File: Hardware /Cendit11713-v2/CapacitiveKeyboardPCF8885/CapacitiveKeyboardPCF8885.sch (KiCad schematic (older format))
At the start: 58 parts

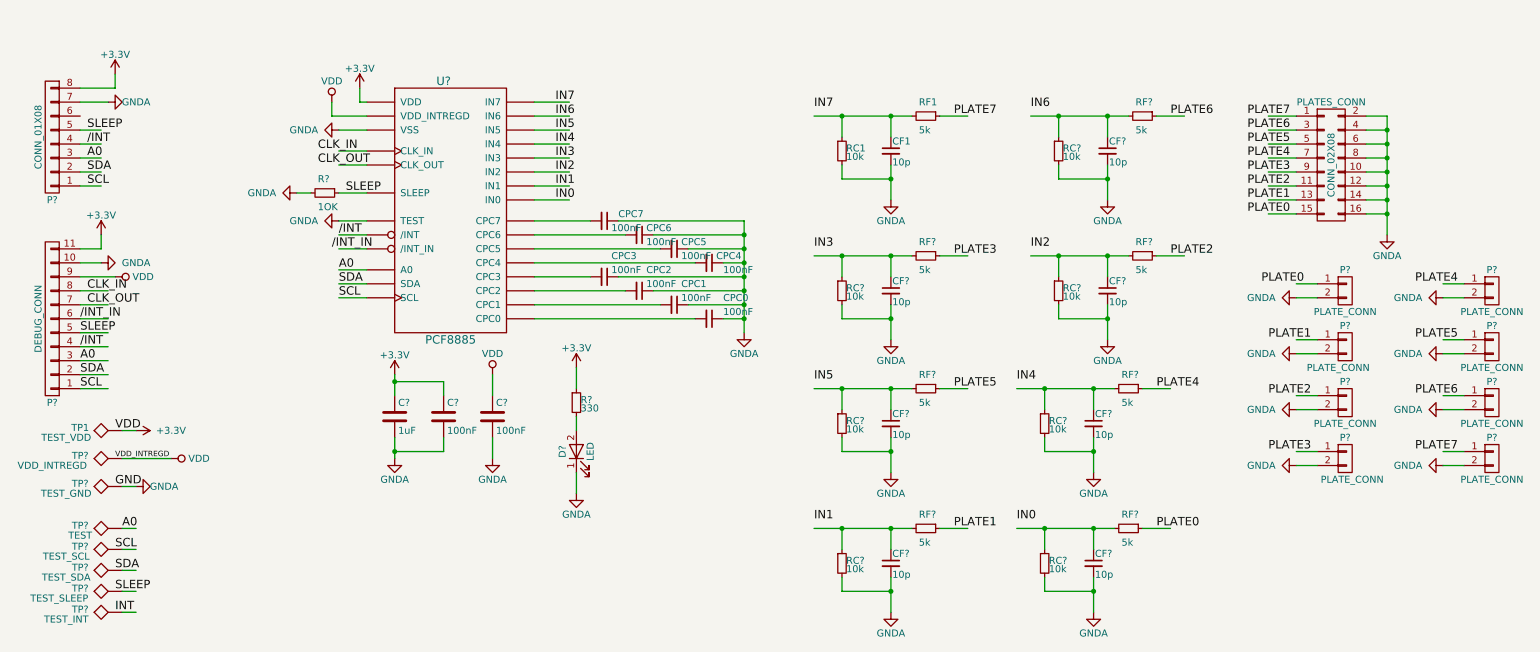
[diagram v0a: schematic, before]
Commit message: Trabajo en CenditLab.Reducido + Cendit17713 PCB
  - Clases paneles UI modificados
  - Clases para manejo y validacion de datos
  - PCB expansor puertos Viking
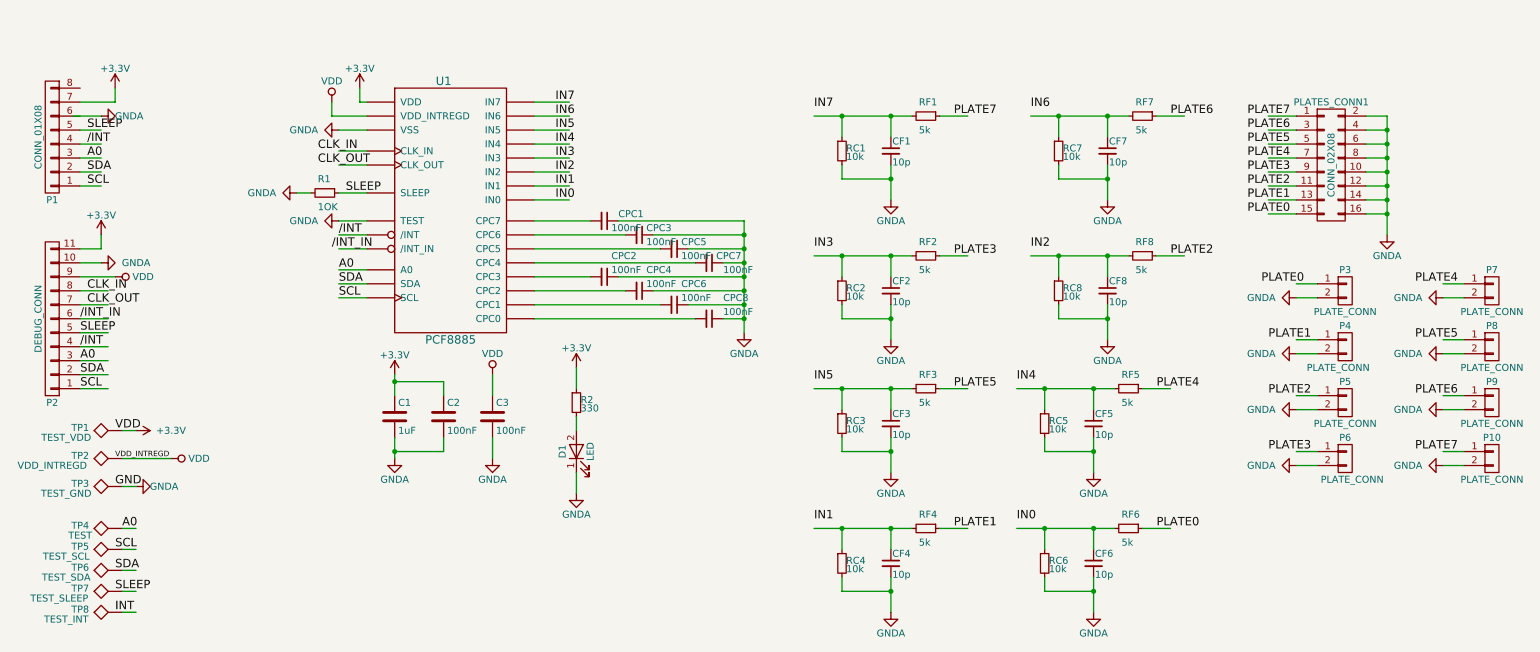
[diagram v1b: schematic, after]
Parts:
- U1: renamed from U?; footprint (none) -> LibKicad:PCF8885TS
- gave numbers to parts that had none: 44
- renumbered CPC7 to CPC1, CPC3 to CPC2, CPC6 to CPC3, CPC2 to CPC4, CPC1 to CPC6, CPC4 to CPC7, CPC0 to CPC8, PLATES_CONN to PLATES_CONN1

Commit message: Trabajo en CenditLab + Cendit11713 PCB
  - Clases UI entrada de ENR + archivos fxml
  - Expansor puertos Viking
  - Controlador teclado capacitivo
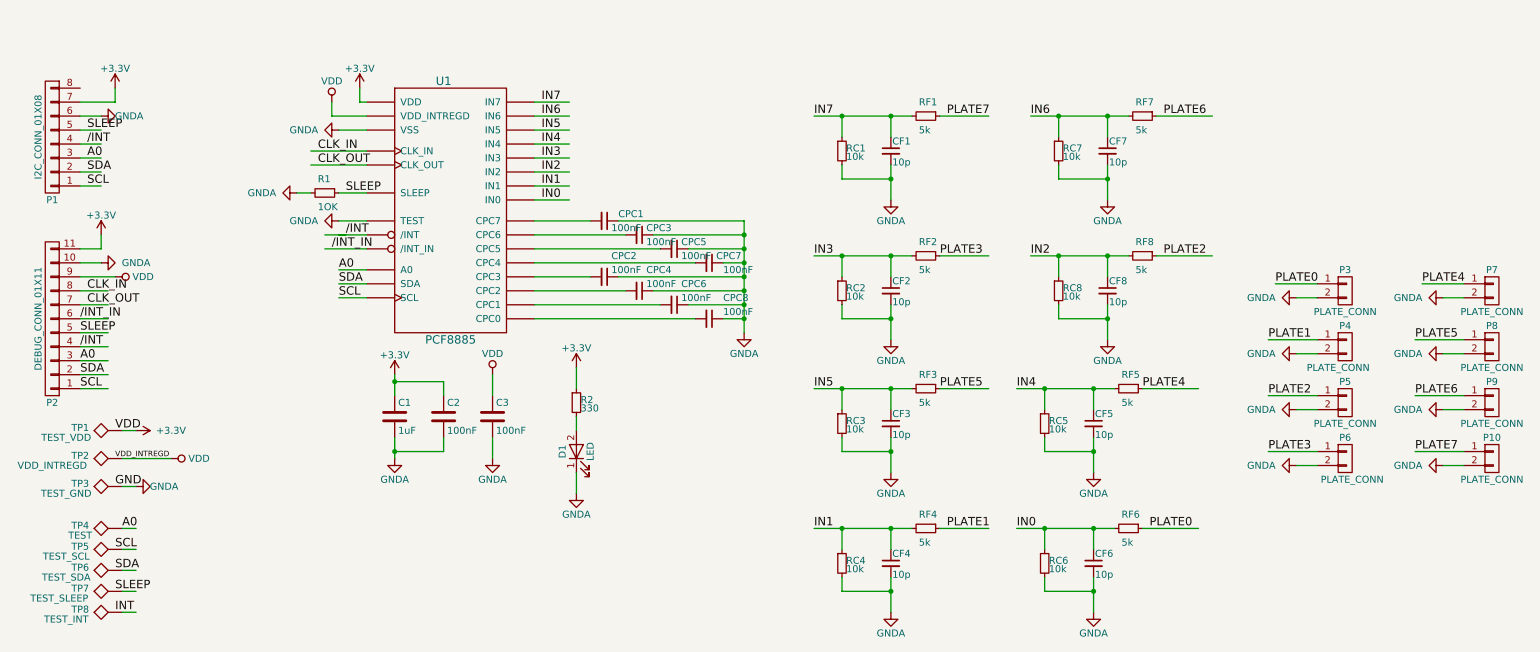
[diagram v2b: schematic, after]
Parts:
- removed PLATES_CONN1: CONN_02X08, symbol CONN_02X08
- C1, C2, C3, CF1, CF2, CF3, CF4, CF5, CF6, CF7, CF8, CPC1, CPC2, CPC3, CPC4, CPC5, CPC6, CPC7, CPC8: footprint (none) -> Capacitors_SMD:C_0805_HandSoldering
- D1: footprint (none) -> LEDs:LED_0805
- P1: value CONN_01X08 -> I2C_CONN_01X08; footprint (none) -> CenditFootprints:SLIMLINE_SATA_PLUG_7P_6P
- P10, P3, P4, P5, P6, P7, P8, P9: footprint (none) -> Pin_Headers:Pin_Header_Straight_1x02
- P2: value DEBUG_CONN -> DEBUG_CONN_01X11; footprint (none) -> Pin_Headers:Pin_Header_Straight_1x11
- R1, R2, RC1, RC2, RC3, RC4, RC5, RC6, RC7, RC8, RF1, RF2, RF3, RF4, RF5, RF6, RF7, RF8: footprint (none) -> Resistors_SMD:R_0805_HandSoldering
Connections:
- wire segments 168 -> 152

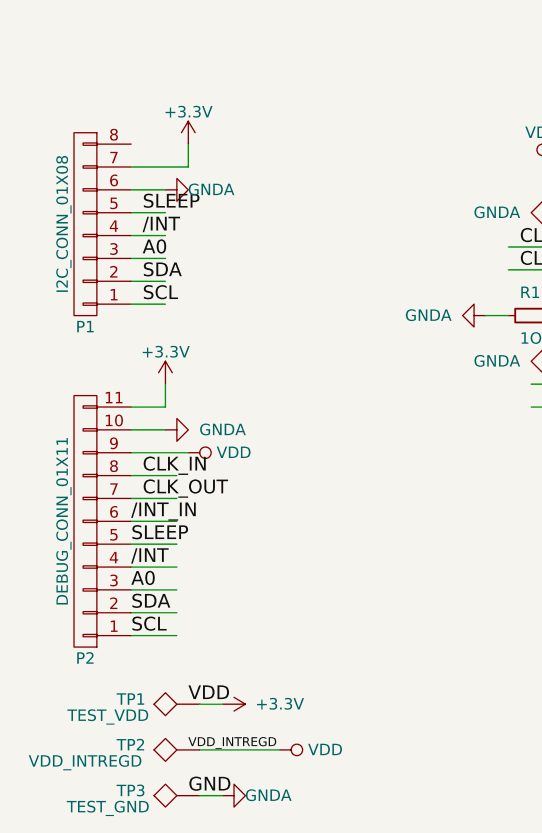
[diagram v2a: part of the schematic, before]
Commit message: Trabajo en CenditLab.Reducido + Cendit11713 PCB
   - CenditLab clases para manejo de setup ENR
   - Clase field para dato temperatura
   - Edición de PCBs Capacitive Keyboard
   - Edición de esquematico MainBoard con PIC18F4550 DIP
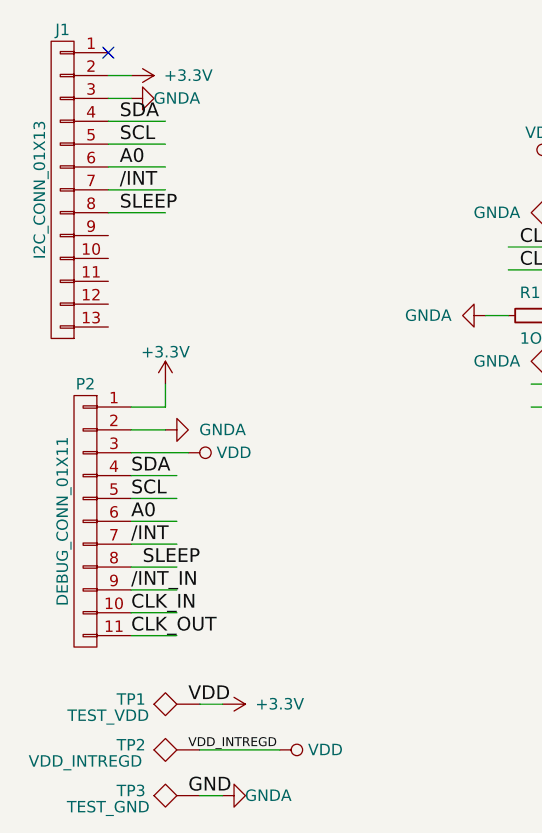
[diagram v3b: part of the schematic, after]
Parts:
- removed P1: I2C_CONN_01X08, CenditFootprints:SLIMLINE_SATA_PLUG_7P_6P, symbol CONN_01X08
- added J1: I2C_CONN_01X13, CenditFootprints:SLIMLINE_SATA_PLUG_7P_6P, symbol CONN_01X13
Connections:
- wire segments 152 -> 151
- no-connect marks 0 -> 1
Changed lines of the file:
@@
 LIBS:contrib
 LIBS:valves
-LIBS:CenditBasic
 LIBS:CapacitiveKeyboardPCF8885-cache
 EELAYER 25 0
@@
 $EndComp
 $Comp
-L GNDA #PWR012
+L GNDA #PWR011
 U 1 1 59CC7E9D
 P 2800 2050
-F 0 "#PWR012" H 2800 1800 50  0001 C CNN
+F 0 "#PWR011" H 2800 1800 50  0001 C CNN
 F 1 "GNDA" V 2800 1800 50  0000 C CNN
 F 2 "" H 2800 2050 50  0000 C CNN
@@
 $EndComp
 $Comp
-L +3.3V #PWR013
+L +3.3V #PWR012
 U 1 1 59CC8C35
 P 2950 1100
-F 0 "#PWR013" H 2950 950 50  0001 C CNN
+F 0 "#PWR012" H 2950 950 50  0001 C CNN
 F 1 "+3.3V" H 2950 1240 50  0000 C CNN
 F 2 "" H 2950 1100 50  0000 C CNN
@@
 $EndComp
 $Comp
-L VDD #PWR014
+L VDD #PWR013
 U 1 1 59CC8CA3
 P 2750 1200
-F 0 "#PWR014" H 2750 1050 50  0001 C CNN
+F 0 "#PWR013" H 2750 1050 50  0001 C CNN
 F 1 "VDD" H 2750 1350 50  0000 C CNN
 F 2 "" H 2750 1200 50  0000 C CNN
@@
 $EndComp
 $Comp
-L +3.3V #PWR015
+L +3.3V #PWR014
 U 1 1 59CCAF94
 P 3200 3150
-F 0 "#PWR015" H 3200 3000 50  0001 C CNN
+F 0 "#PWR014" H 3200 3000 50  0001 C CNN
 F 1 "+3.3V" H 3200 3290 50  0000 C CNN
 F 2 "" H 3200 3150 50  0000 C CNN
@@
 $EndComp
 $Comp
-L VDD #PWR016
+L VDD #PWR015
 U 1 1 59CCB002
 P 3900 3150
-F 0 "#PWR016" H 3900 3000 50  0001 C CNN
+F 0 "#PWR015" H 3900 3000 50  0001 C CNN
 F 1 "VDD" H 3900 3300 50  0000 C CNN
 F 2 "" H 3900 3150 50  0000 C CNN
@@
 $EndComp
 $Comp
-L GNDA #PWR017
+L GNDA #PWR016
 U 1 1 59CCB3D4
 P 3200 3750
-F 0 "#PWR017" H 3200 3500 50  0001 C CNN
+F 0 "#PWR016" H 3200 3500 50  0001 C CNN
 F 1 "GNDA" H 3200 3600 50  0000 C CNN
 F 2 "" H 3200 3750 50  0000 C CNN
@@
 $EndComp
 $Comp
-L GNDA #PWR018
+L GNDA #PWR017
 U 1 1 59CCB46F
 P 3900 3750
-F 0 "#PWR018" H 3900 3500 50  0001 C CNN
+F 0 "#PWR017" H 3900 3500 50  0001 C CNN
 F 1 "GNDA" H 3900 3600 50  0000 C CNN
 F 2 "" H 3900 3750 50  0000 C CNN
@@
 $EndComp
 $Comp
-L GNDA #PWR019
+L GNDA #PWR018
 U 1 1 59CDAF81
 P 9650 3800
-F 0 "#PWR019" H 9650 3550 50  0001 C CNN
+F 0 "#PWR018" H 9650 3550 50  0001 C CNN
 F 1 "GNDA" V 9650 3550 50  0000 C CNN
 F 2 "" H 9650 3800 50  0000 C CNN
@@
 $EndComp
 $Comp
-L GNDA #PWR020
+L GNDA #PWR019
 U 1 1 59CDAFEF
 P 9650 3400
-F 0 "#PWR020" H 9650 3150 50  0001 C CNN
+F 0 "#PWR019" H 9650 3150 50  0001 C CNN
 F 1 "GNDA" V 9650 3150 50  0000 C CNN
 F 2 "" H 9650 3400 50  0000 C CNN
@@
 $EndComp
 $Comp
-L GNDA #PWR021
+L GNDA #PWR020
 U 1 1 59CDB364
 P 9650 3000
-F 0 "#PWR021" H 9650 2750 50  0001 C CNN
+F 0 "#PWR020" H 9650 2750 50  0001 C CNN
 F 1 "GNDA" V 9650 2750 50  0000 C CNN
 F 2 "" H 9650 3000 50  0000 C CNN
@@
 $EndComp
 $Comp
-L GNDA #PWR022
+L GNDA #PWR021
 U 1 1 59CDB3D2
 P 9650 2600
-F 0 "#PWR022" H 9650 2350 50  0001 C CNN
+F 0 "#PWR021" H 9650 2350 50  0001 C CNN
 F 1 "GNDA" V 9650 2350 50  0000 C CNN
 F 2 "" H 9650 2600 50  0000 C CNN
@@
 $EndComp
 $Comp
-L GNDA #PWR023
+L GNDA #PWR022
 U 1 1 59CDBC01
 P 10700 2600
-F 0 "#PWR023" H 10700 2350 50  0001 C CNN
+F 0 "#PWR022" H 10700 2350 50  0001 C CNN
 F 1 "GNDA" V 10700 2350 50  0000 C CNN
 F 2 "" H 10700 2600 50  0000 C CNN
@@
 $EndComp
 $Comp
-L GNDA #PWR024
+L GNDA #PWR023
 U 1 1 59CDBC6F
 P 10700 3000
-F 0 "#PWR024" H 10700 2750 50  0001 C CNN
+F 0 "#PWR023" H 10700 2750 50  0001 C CNN
 F 1 "GNDA" V 10700 2750 50  0000 C CNN
 F 2 "" H 10700 3000 50  0000 C CNN
@@
 $EndComp
 $Comp
-L GNDA #PWR025
+L GNDA #PWR024
 U 1 1 59CDBD37
 P 10700 3400
-F 0 "#PWR025" H 10700 3150 50  0001 C CNN
+F 0 "#PWR024" H 10700 3150 50  0001 C CNN
 F 1 "GNDA" V 10700 3150 50  0000 C CNN
 F 2 "" H 10700 3400 50  0000 C CNN
@@
 $EndComp
 $Comp
-L GNDA #PWR026
+L GNDA #PWR025
 U 1 1 59CDBDFF
 P 10700 3800
-F 0 "#PWR026" H 10700 3550 50  0001 C CNN
+F 0 "#PWR025" H 10700 3550 50  0001 C CNN
 F 1 "GNDA" V 10700 3550 50  0000 C CNN
 F 2 "" H 10700 3800 50  0000 C CNN
@@
 PLATE7
 $Comp
-L CONN_01X08 P1
-U 1 1 59CE24CF
-P 750 1450
-F 0 "P1" H 750 1900 50  0000 C CNN
-F 1 "I2C_CONN_01X08" V 850 1450 50  0000 C CNN
-F 2 "CenditFootprints:SLIMLINE_SATA_PLUG_7P_6P" H 750 1450 50  0001 C CNN
-F 3 "" H 750 1450 50  0000 C CNN
-	1    750  1450
-	-1   0    0    1
-$EndComp
-$Comp
 L CONN_01X11 P2
 U 1 1 59CE30AA
@@
 F 3 "" H 750 2750 50  0000 C CNN
 	1    750  2750
-	-1   0    0    1
-$EndComp
-$Comp
-L GNDA #PWR027
+	-1   0    0    -1
+$EndComp
+$Comp
+L GNDA #PWR026
 U 1 1 59CE507F
-P 1100 1300
-F 0 "#PWR027" H 1100 1050 50  0001 C CNN
-F 1 "GNDA" V 1100 1100 50  0000 C CNN
-F 2 "" H 1100 1300 50  0000 C CNN
-F 3 "" H 1100 1300 50  0000 C CNN
-	1    1100 1300
+P 950 900
+F 0 "#PWR026" H 950 650 50  0001 C CNN
+F 1 "GNDA" V 950 700 50  0000 C CNN
+F 2 "" H 950 900 50  0000 C CNN
+F 3 "" H 950 900 50  0000 C CNN
+	1    950  900
 	0    -1   -1   0
 $EndComp
 $Comp
-L +3.3V #PWR028
+L +3.3V #PWR027
 U 1 1 59CE5337
-P 1200 1100
-F 0 "#PWR028" H 1200 950 50  0001 C CNN
-F 1 "+3.3V" H 1200 1240 50  0000 C CNN
-F 2 "" H 1200 1100 50  0000 C CNN
-F 3 "" H 1200 1100 50  0000 C CNN
-	1    1200 1100
-	1    0    0    -1
-$EndComp
-Text Label 1000 1800 0    60   ~ 0
+P 950 800
+F 0 "#PWR027" H 950 650 50  0001 C CNN
+F 1 "+3.3V" V 950 1050 50  0000 C CNN
+F 2 "" H 950 800 50  0000 C CNN
+F 3 "" H 950 800 50  0000 C CNN
+	1    950  800
+	0    1    1    0
+$EndComp
+Text Label 900  1100 0    60   ~ 0
 SCL
-Text Label 1000 1700 0    60   ~ 0
+Text Label 900  1000 0    60   ~ 0
 SDA
-Text Label 1000 1600 0    60   ~ 0
+Text Label 900  1200 0    60   ~ 0
 A0
-Text Label 1000 1500 0    60   ~ 0
+Text Label 900  1300 0    60   ~ 0
 /INT
-Text Label 1000 1400 0    60   ~ 0
+Text Label 900  1400 0    60   ~ 0
 SLEEP
 $Comp
@@
 $EndComp
 $Comp
-L GNDA #PWR029
+L GNDA #PWR028
 U 1 1 59CE74DE
 P 2500 1850
-F 0 "#PWR029" H 2500 1600 50  0001 C CNN
+F 0 "#PWR028" H 2500 1600 50  0001 C CNN
 F 1 "GNDA" V 2500 1600 50  0000 C CNN
 F 2 "" H 2500 1850 50  0000 C CNN
@@
 SLEEP
 $Comp
-L +3.3V #PWR030
+L +3.3V #PWR029
 U 1 1 59CEC609
 P 1100 2150
-F 0 "#PWR030" H 1100 2000 50  0001 C CNN
+F 0 "#PWR029" H 1100 2000 50  0001 C CNN
 F 1 "+3.3V" H 1100 2290 50  0000 C CNN
 F 2 "" H 1100 2150 50  0000 C CNN
@@
 $EndComp
 $Comp
-L GNDA #PWR031
+L GNDA #PWR030
 U 1 1 59CEC67D
 P 1100 2350
-F 0 "#PWR031" H 1100 2100 50  0001 C CNN
+F 0 "#PWR030" H 1100 2100 50  0001 C CNN
 F 1 "GNDA" V 1100 2100 50  0000 C CNN
 F 2 "" H 1100 2350 50  0000 C CNN
@@
 $EndComp
 $Comp
-L VDD #PWR032
+L VDD #PWR031
 U 1 1 59CECB1B
 P 1200 2450
-F 0 "#PWR032" H 1200 2300 50  0001 C CNN
+F 0 "#PWR031" H 1200 2300 50  0001 C CNN
 F 1 "VDD" V 1200 2650 50  0000 C CNN
 F 2 "" H 1200 2450 50  0000 C CNN
@@
 Text Label 2650 1550 0    60   ~ 0
 CLK_IN
+Text Label 950  2650 0    60   ~ 0
+SCL
+Text Label 950  2550 0    60   ~ 0
+SDA
+Text Label 950  2750 0    60   ~ 0
+A0
+Text Label 950  2850 0    60   ~ 0
+/INT
+Text Label 1000 2950 0    60   ~ 0
+SLEEP
+Text Label 950  3050 0    60   ~ 0
+/INT_IN
+Text Label 950  3150 0    60   ~ 0
+CLK_IN
 Text Label 950  3250 0    60   ~ 0
-SCL
-Text Label 950  3150 0    60   ~ 0
-SDA
-Text Label 950  3050 0    60   ~ 0
-A0
-Text Label 950  2950 0    60   ~ 0
-/INT
-Text Label 950  2850 0    60   ~ 0
-SLEEP
-Text Label 950  2750 0    60   ~ 0
-/INT_IN
-Text Label 1000 2550 0    60   ~ 0
-CLK_IN
-Text Label 1000 2650 0    60   ~ 0
 CLK_OUT
 $Comp
@@
 $EndComp
 $Comp
-L +3.3V #PWR033
+L +3.3V #PWR032
 U 1 1 59CFAFA9
 P 4500 3100
-F 0 "#PWR033" H 4500 2950 50  0001 C CNN
+F 0 "#PWR032" H 4500 2950 50  0001 C CNN
 F 1 "+3.3V" H 4500 3240 50  0000 C CNN
 F 2 "" H 4500 3100 50  0000 C CNN
@@
 $EndComp
 $Comp
-L GNDA #PWR034
+L GNDA #PWR033
 U 1 1 59CFB085
 P 4500 4000
-F 0 "#PWR034" H 4500 3750 50  0001 C CNN
+F 0 "#PWR033" H 4500 3750 50  0001 C CNN
 F 1 "GNDA" H 4500 3850 50  0000 C CNN
 F 2 "" H 4500 4000 50  0000 C CNN
@@
 GND
 $Comp
-L GNDA #PWR035
+L GNDA #PWR034
 U 1 1 59D0D18F
 P 1350 3950
-F 0 "#PWR035" H 1350 3700 50  0001 C CNN
+F 0 "#PWR034" H 1350 3700 50  0001 C CNN
 F 1 "GNDA" V 1350 3750 50  0000 C CNN
 F 2 "" H 1350 3950 50  0000 C CNN
@@
 $EndComp
 $Comp
-L +3.3V #PWR036
+L +3.3V #PWR035
 U 1 1 59D0D3EE
 P 1350 3550
-F 0 "#PWR036" H 1350 3400 50  0001 C CNN
+F 0 "#PWR035" H 1350 3400 50  0001 C CNN
 F 1 "+3.3V" V 1350 3800 50  0000 C CNN
 F 2 "" H 1350 3550 50  0000 C CNN
@@
 $EndComp
 $Comp
-L VDD #PWR037
+L VDD #PWR036
 U 1 1 59D0D5CE
 P 1600 3750
-F 0 "#PWR037" H 1600 3600 50  0001 C CNN
+F 0 "#PWR036" H 1600 3600 50  0001 C CNN
 F 1 "VDD" V 1600 3950 50  0000 C CNN
 F 2 "" H 1600 3750 50  0000 C CNN
@@
 	9800 2600 9650 2600
 Wire Wire Line
-	950  1200 1200 1200
-Wire Wire Line
-	950  1400 1100 1400
-Wire Wire Line
-	950  1500 1100 1500
-Wire Wire Line
-	950  1600 1100 1600
-Wire Wire Line
-	950  1700 1100 1700
-Wire Wire Line
-	950  1800 1100 1800
-Wire Wire Line
 	2600 1550 3000 1550
 Wire Wire Line
@@
 	3000 2600 2800 2600
 Wire Wire Line
-	1200 1200 1200 1100
-Wire Wire Line
 	2800 1850 3000 1850
 Wire Wire Line
@@
 	2850 2150 2700 2150
 Wire Wire Line
-	1100 1300 950  1300
-Wire Wire Line
 	10850 3700 10500 3700
 Wire Wire Line
 	10850 2500 10550 2500
+NoConn ~ 850  700
+$Comp
+L CONN_01X13 J1
+U 1 1 59E66F43
+P 650 1300
+F 0 "J1" H 650 2000 50  0000 C CNN
+F 1 "I2C_CONN_01X13" V 750 1300 50  0000 C CNN
+F 2 "CenditFootprints:SLIMLINE_SATA_PLUG_7P_6P" H 650 1300 50  0001 C CNN
+F 3 "" H 650 1300 50  0001 C CNN
+	1    650  1300
+	-1   0    0    -1
+$EndComp
+Wire Wire Line
+	850  800  950  800
+Wire Wire Line
+	850  900  950  900
+Wire Wire Line
+	850  1000 1100 1000
+Wire Wire Line
+	850  1100 1100 1100
+Wire Wire Line
+	850  1200 1100 1200
+Wire Wire Line
+	850  1300 1100 1300
+Wire Wire Line
+	850  1400 1100 1400
 $EndSCHEMATC

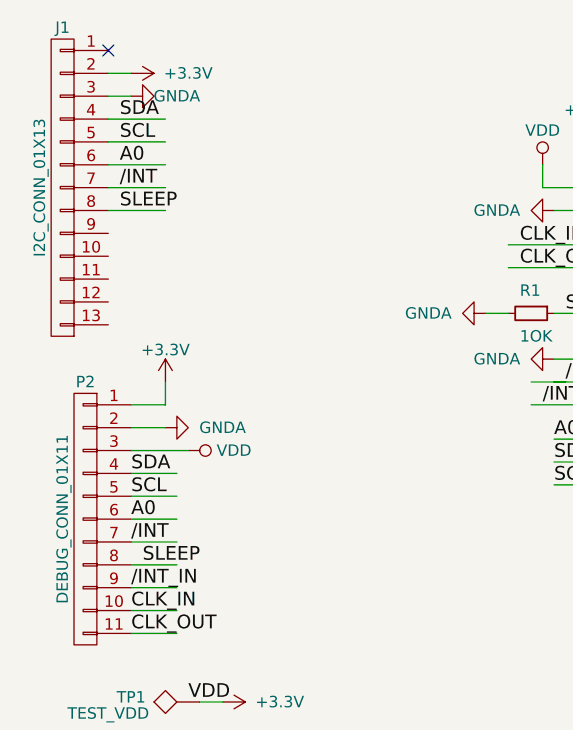
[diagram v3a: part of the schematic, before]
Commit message: Trabajo en Cendit11713
  - Revision de esquematicos + PCBs
  - Generacion de archivos Gerber
  - CapacitiveKeyboard -> edicion PCB
  - Inicia PCB GpibPortExpander
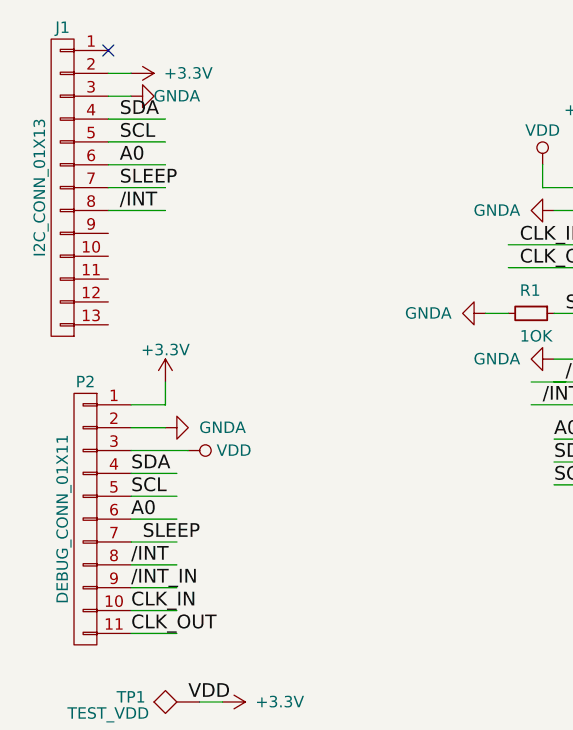
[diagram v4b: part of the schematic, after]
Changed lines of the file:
@@
 LIBS:contrib
 LIBS:valves
+LIBS:CenditBasic
 LIBS:CapacitiveKeyboardPCF8885-cache
 EELAYER 25 0
@@
 Text Label 900  1200 0    60   ~ 0
 A0
+Text Label 900  1400 0    60   ~ 0
+/INT
 Text Label 900  1300 0    60   ~ 0
-/INT
-Text Label 900  1400 0    60   ~ 0
 SLEEP
 $Comp
@@
 Text Label 950  2750 0    60   ~ 0
 A0
-Text Label 950  2850 0    60   ~ 0
+Text Label 950  2950 0    60   ~ 0
 /INT
-Text Label 1000 2950 0    60   ~ 0
+Text Label 1000 2850 0    60   ~ 0
 SLEEP
 Text Label 950  3050 0    60   ~ 0

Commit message: En Cendit11713 edicion de esquematicos + revision PCBs
  - Edicion de esquematicos tarjeta madre
  - Revision de PCBs corrección de footprints
  - Descarga de footprints + creacion lib simbolos: RTC + sensor temp/hum
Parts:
- U1: footprint LibKicad:PCF8885TS -> LibreriaKicad2:PCF8885TS
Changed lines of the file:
@@
 F 0 "U1" H 3550 2550 60  0000 C CNN
 F 1 "PCF8885" H 3600 700 60  0000 C CNN
-F 2 "LibKicad:PCF8885TS" H 3400 1800 60  0001 C CNN
+F 2 "LibreriaKicad2:PCF8885TS" H 3400 1800 60  0001 C CNN
 F 3 "" H 3400 1800 60  0001 C CNN
 	1    3400 1800
